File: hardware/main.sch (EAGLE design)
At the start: 9 parts, among them IC1 AZ1117

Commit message: 5Vの電源含めて試作回路図完成
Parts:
- added C1, C2: (no value), resistor:CPOL-EUE5-10.5
- added D2: 1N4933, diode:1N4933
- added L1: (no value), resistor:L-EU0207/10
- added U$1: SI-8050S, con-user:SI-8050S
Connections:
- new net +5V: C2.+, JP2.1, L1.2, U$1.VOS, X1.1
- new net N$4: D2.C, L1.1, U$1.SWOUT
- net GND: now also C1.-, C2.-, D2.A, JP2.2, U$1.GND, X1.4
- net N$5: now also C1.+, U$1.VIN
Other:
- moved on the sheet: JP2, X1
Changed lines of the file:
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@@
 <layer number="97" name="Info" color="7" fill="1" visible="yes" active="yes"/>
 <layer number="98" name="Guide" color="6" fill="1" visible="yes" active="yes"/>
+<layer number="99" name="SpiceOrder" color="5" fill="1" visible="yes" active="yes"/>
 </layers>
 <schematic xreflabel="%F%N/%S.%C%R" xrefpart="/%S.%C%R">
@@
 <part name="GND3" library="supply1" deviceset="GND" device=""/>
 <part name="G1" library="battery" deviceset="AB9V" device="" value="NiMH Battery 8.4V"/>
+<part name="P+1" library="supply1" deviceset="+5V" device=""/>
+<part name="P+2" library="supply1" deviceset="+5V" device=""/>
+<part name="GND4" library="supply1" deviceset="GND" device=""/>
+<part name="U$1" library="con-user" deviceset="SI-8050S" device=""/>
+<part name="C1" library="resistor" deviceset="CPOL-EU" device="E5-10.5"/>
+<part name="C2" library="resistor" deviceset="CPOL-EU" device="E5-10.5"/>
+<part name="D2" library="diode" deviceset="1N4933" device=""/>
+<part name="L1" library="resistor" deviceset="L-EU" device="0207/10"/>
+<part name="GND5" library="supply1" deviceset="GND" device=""/>
+<part name="GND6" library="supply1" deviceset="GND" device=""/>
+<part name="GND7" library="supply1" deviceset="GND" device=""/>
+<part name="GND8" library="supply1" deviceset="GND" device=""/>
+<part name="P+3" library="supply1" deviceset="+5V" device=""/>
 </parts>
 <sheets>
@@
 <instance part="D4" gate="G$1" x="101.6" y="78.74"/>
 <instance part="JP1" gate="G$1" x="5.08" y="45.72" rot="MR0"/>
-<instance part="JP2" gate="G$1" x="162.56" y="45.72"/>
-<instance part="X1" gate="G$1" x="157.48" y="27.94"/>
+<instance part="JP2" gate="G$1" x="259.08" y="63.5"/>
+<instance part="X1" gate="G$1" x="248.92" y="30.48"/>
 <instance part="GND1" gate="1" x="15.24" y="30.48"/>
 <instance part="GND2" gate="1" x="99.06" y="17.78"/>
-<instance part="GND3" gate="1" x="121.92" y="20.32"/>
+<instance part="GND3" gate="1" x="241.3" y="22.86"/>
 <instance part="G1" gate="G$1" x="99.06" y="35.56" rot="R90"/>
+<instance part="P+1" gate="1" x="241.3" y="45.72"/>
+<instance part="P+2" gate="1" x="246.38" y="76.2"/>
+<instance part="GND4" gate="1" x="246.38" y="55.88"/>
+<instance part="U$1" gate="G$1" x="160.02" y="45.72"/>
+<instance part="C1" gate="G$1" x="129.54" y="33.02"/>
+<instance part="C2" gate="G$1" x="205.74" y="38.1"/>
+<instance part="D2" gate="1" x="182.88" y="35.56" rot="R90"/>
+<instance part="L1" gate="G$1" x="190.5" y="48.26" rot="R90"/>
+<instance part="GND5" gate="1" x="129.54" y="20.32"/>
+<instance part="GND6" gate="1" x="160.02" y="22.86"/>
+<instance part="GND7" gate="1" x="182.88" y="22.86"/>
+<instance part="GND8" gate="1" x="205.74" y="22.86"/>
+<instance part="P+3" gate="1" x="205.74" y="55.88"/>
 </instances>
 <busses>
@@
 <pinref part="D3" gate="G$1" pin="C"/>
 <wire x1="119.38" y1="48.26" x2="111.76" y2="48.26" width="0.1524" layer="91"/>
+<pinref part="U$1" gate="G$1" pin="VIN"/>
+<wire x1="119.38" y1="48.26" x2="129.54" y2="48.26" width="0.1524" layer="91"/>
+<junction x="119.38" y="48.26"/>
+<pinref part="C1" gate="G$1" pin="+"/>
+<wire x1="129.54" y1="48.26" x2="142.24" y2="48.26" width="0.1524" layer="91"/>
+<wire x1="129.54" y1="35.56" x2="129.54" y2="48.26" width="0.1524" layer="91"/>
+<junction x="129.54" y="48.26"/>
 </segment>
 </net>
@@
 <wire x1="99.06" y1="20.32" x2="99.06" y2="22.86" width="0.1524" layer="91"/>
 </segment>
-</net>
+<segment>
+<pinref part="GND3" gate="1" pin="GND"/>
+<pinref part="X1" gate="G$1" pin="4"/>
+<wire x1="241.3" y1="25.4" x2="241.3" y2="27.94" width="0.1524" layer="91"/>
+<wire x1="241.3" y1="27.94" x2="246.38" y2="27.94" width="0.1524" layer="91"/>
+</segment>
+<segment>
+<pinref part="GND4" gate="1" pin="GND"/>
+<pinref part="JP2" gate="G$1" pin="2"/>
+<wire x1="246.38" y1="58.42" x2="246.38" y2="63.5" width="0.1524" layer="91"/>
+<wire x1="246.38" y1="63.5" x2="256.54" y2="63.5" width="0.1524" layer="91"/>
+</segment>
+<segment>
+<pinref part="C1" gate="G$1" pin="-"/>
+<pinref part="GND5" gate="1" pin="GND"/>
+<wire x1="129.54" y1="27.94" x2="129.54" y2="22.86" width="0.1524" layer="91"/>
+</segment>
+<segment>
+<pinref part="U$1" gate="G$1" pin="GND"/>
+<pinref part="GND6" gate="1" pin="GND"/>
+<wire x1="160.02" y1="33.02" x2="160.02" y2="25.4" width="0.1524" layer="91"/>
+</segment>
+<segment>
+<pinref part="D2" gate="1" pin="A"/>
+<pinref part="GND7" gate="1" pin="GND"/>
+<wire x1="182.88" y1="33.02" x2="182.88" y2="25.4" width="0.1524" layer="91"/>
+</segment>
+<segment>
+<pinref part="C2" gate="G$1" pin="-"/>
+<pinref part="GND8" gate="1" pin="GND"/>
+<wire x1="205.74" y1="33.02" x2="205.74" y2="25.4" width="0.1524" layer="91"/>
+</segment>
+</net>
+<net name="+5V" class="0">
+<segment>
+<pinref part="P+1" gate="1" pin="+5V"/>
+<pinref part="X1" gate="G$1" pin="1"/>
+<wire x1="241.3" y1="43.18" x2="241.3" y2="35.56" width="0.1524" layer="91"/>
+<wire x1="241.3" y1="35.56" x2="246.38" y2="35.56" width="0.1524" layer="91"/>
+</segment>
+<segment>
+<pinref part="P+2" gate="1" pin="+5V"/>
+<pinref part="JP2" gate="G$1" pin="1"/>
+<wire x1="246.38" y1="73.66" x2="246.38" y2="66.04" width="0.1524" layer="91"/>
+<wire x1="246.38" y1="66.04" x2="256.54" y2="66.04" width="0.1524" layer="91"/>
+</segment>
+<segment>
+<pinref part="U$1" gate="G$1" pin="VOS"/>
+<wire x1="175.26" y1="40.64" x2="177.8" y2="40.64" width="0.1524" layer="91"/>
+<wire x1="177.8" y1="40.64" x2="177.8" y2="53.34" width="0.1524" layer="91"/>
+<wire x1="177.8" y1="53.34" x2="198.12" y2="53.34" width="0.1524" layer="91"/>
+<wire x1="198.12" y1="53.34" x2="198.12" y2="48.26" width="0.1524" layer="91"/>
+<pinref part="L1" gate="G$1" pin="2"/>
+<wire x1="198.12" y1="48.26" x2="195.58" y2="48.26" width="0.1524" layer="91"/>
+<pinref part="C2" gate="G$1" pin="+"/>
+<wire x1="198.12" y1="48.26" x2="205.74" y2="48.26" width="0.1524" layer="91"/>
+<wire x1="205.74" y1="48.26" x2="205.74" y2="40.64" width="0.1524" layer="91"/>
+<junction x="198.12" y="48.26"/>
+<wire x1="205.74" y1="48.26" x2="205.74" y2="53.34" width="0.1524" layer="91"/>
+<junction x="205.74" y="48.26"/>
+<pinref part="P+3" gate="1" pin="+5V"/>
+</segment>
+</net>
+<net name="N$4" class="0">
+<segment>
+<pinref part="U$1" gate="G$1" pin="SWOUT"/>
+<pinref part="L1" gate="G$1" pin="1"/>
+<wire x1="175.26" y1="48.26" x2="182.88" y2="48.26" width="0.1524" layer="91"/>
+<pinref part="D2" gate="1" pin="C"/>
+<wire x1="182.88" y1="48.26" x2="185.42" y2="48.26" width="0.1524" layer="91"/>
+<wire x1="182.88" y1="38.1" x2="182.88" y2="48.26" width="0.1524" layer="91"/>
+<junction x="182.88" y="48.26"/>
+</segment>
+</net>

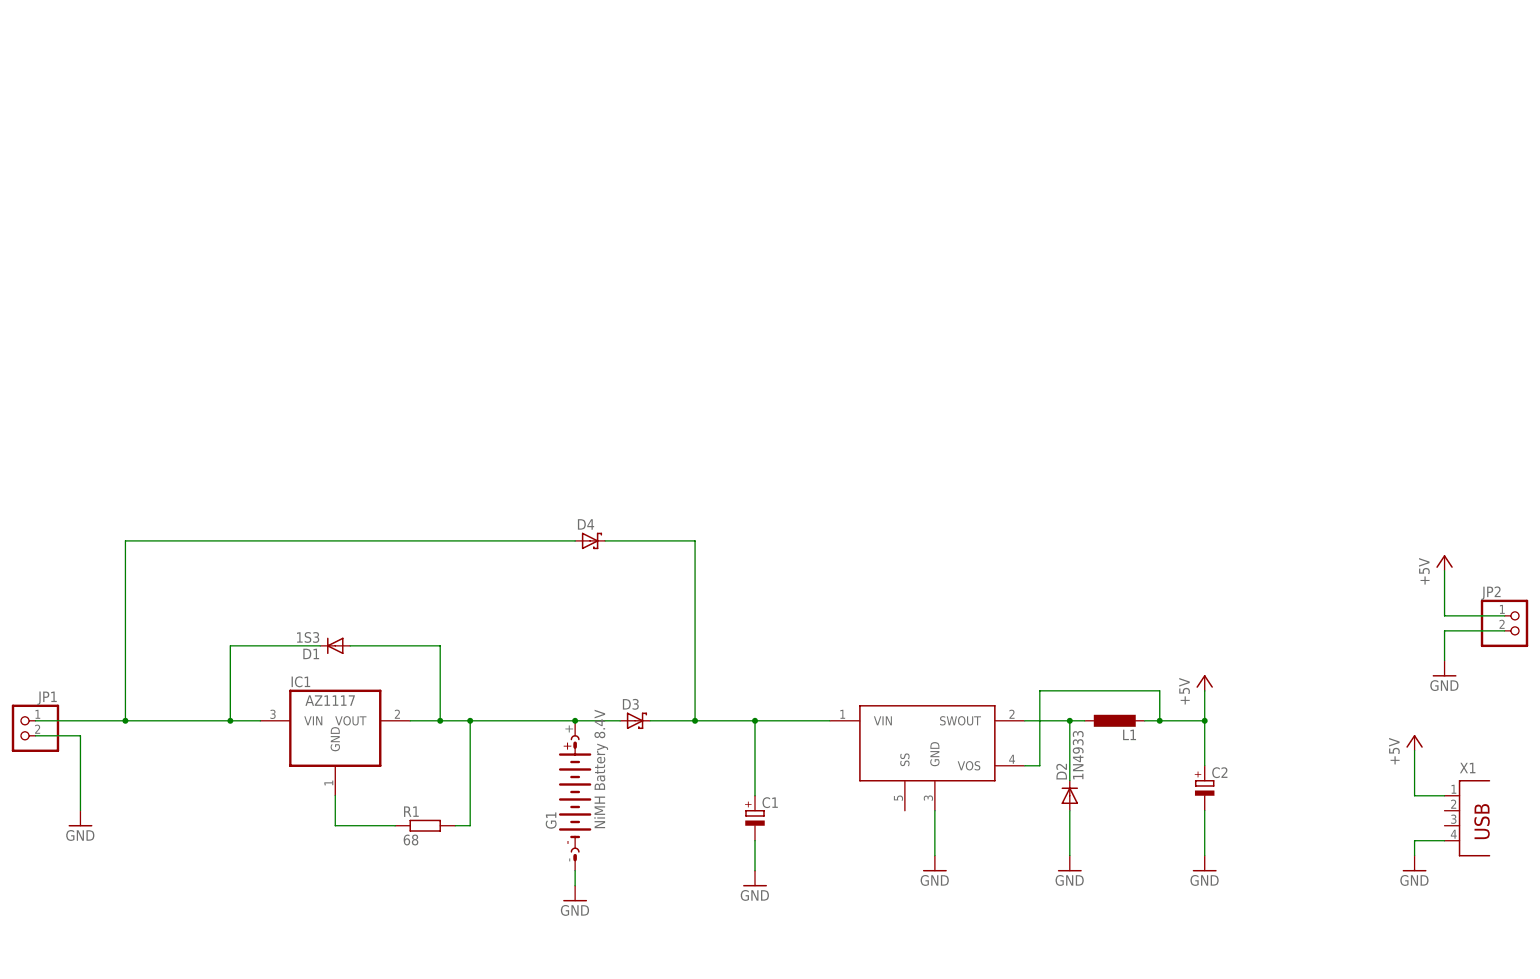
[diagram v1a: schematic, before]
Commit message: 電圧コンパレーター実装 抵抗の場所間違いを修正 試作に合わせて修正
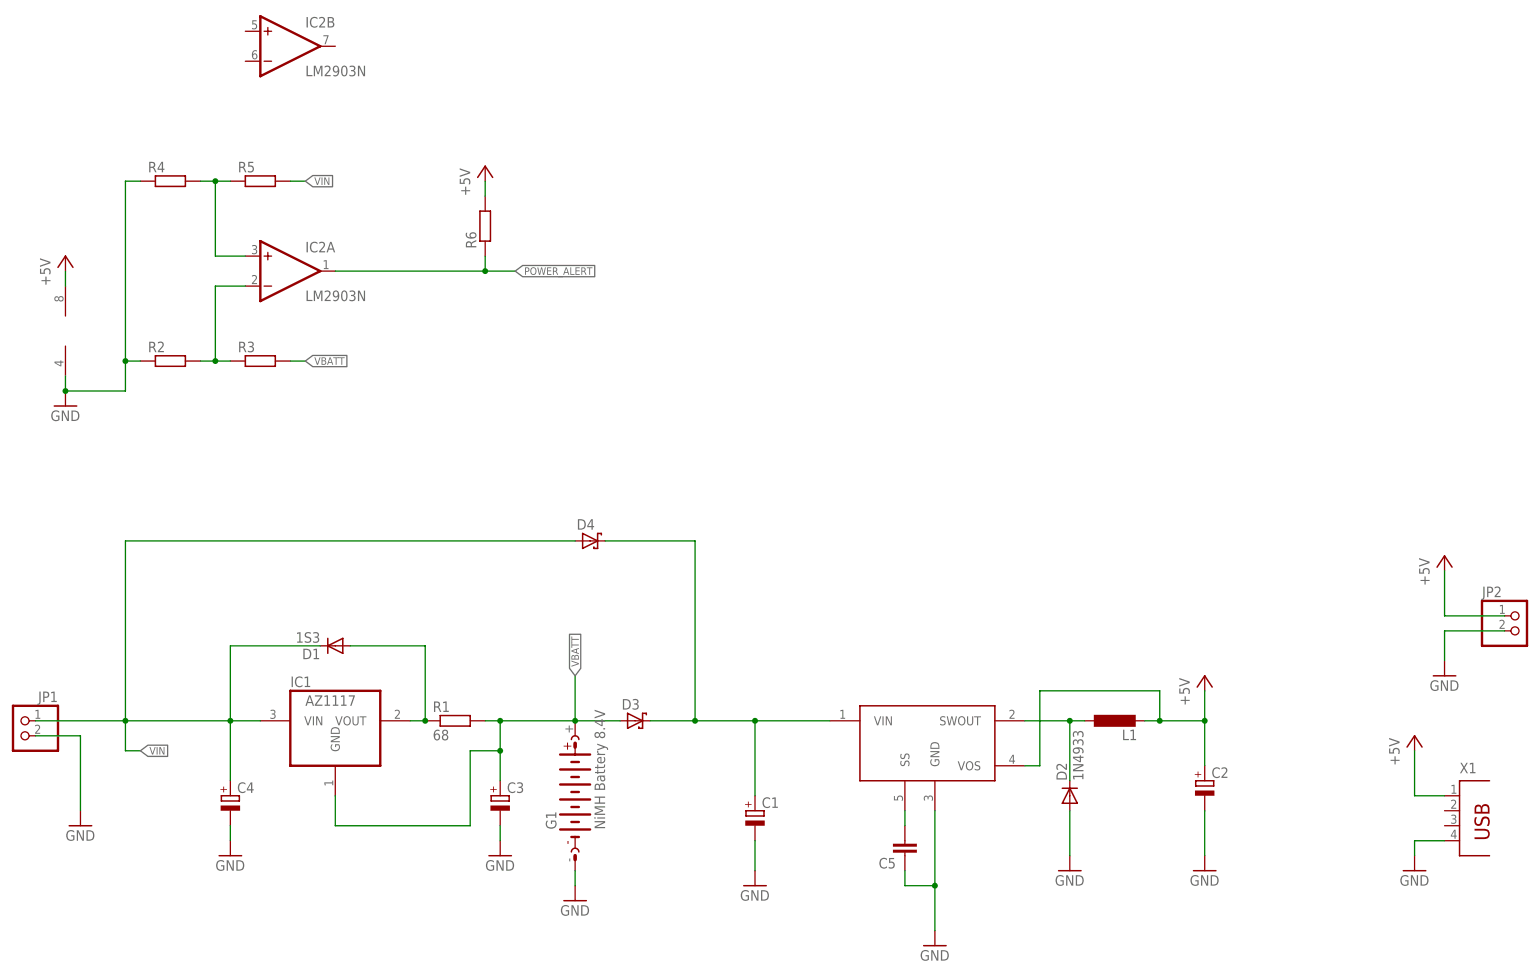
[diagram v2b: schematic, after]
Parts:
- added C3, C4: (no value), resistor:CPOL-EUE5-10.5
- added C5: (no value), resistor:C-EUC0603K
- added IC2: LM2903N, linear:LM2903N
- added R2, R3, R4, R5, R6: (no value), resistor:R-EU_R0603
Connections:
- removed net N$2: D1.A, D3.A, G1.+, IC1.VOUT, R1.2
- new net N$10: IC2A.+IN, R4.2, R5.1
- new net N$6: D1.A, IC1.VOUT, R1.1
- new net POWER_ALERT: IC2A.OUT, R6.1
- new net VBATT: C3.+, D3.A, G1.+, IC1.GND, R1.2, R3.2
- new net VIN: C4.+, D1.C, D4.A, IC1.VIN, JP1.1, R5.2
- net +5V: now also IC2P.V+, R6.2
- net GND: now also C3.-, C4.-, C5.1, IC2P.V-, R2.1, R4.1
- net N$1: now also C5.2, U$1.SS; no longer D1.C, D4.A, IC1.VIN, JP1.1
- net N$3: now also IC2A.-IN, R2.2, R3.1; no longer IC1.GND, R1.1
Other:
- moved on the sheet: R1
